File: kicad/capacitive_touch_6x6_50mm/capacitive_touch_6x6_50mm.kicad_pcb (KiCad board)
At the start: 2 copper layers, 50 x 50 mm, 1 part

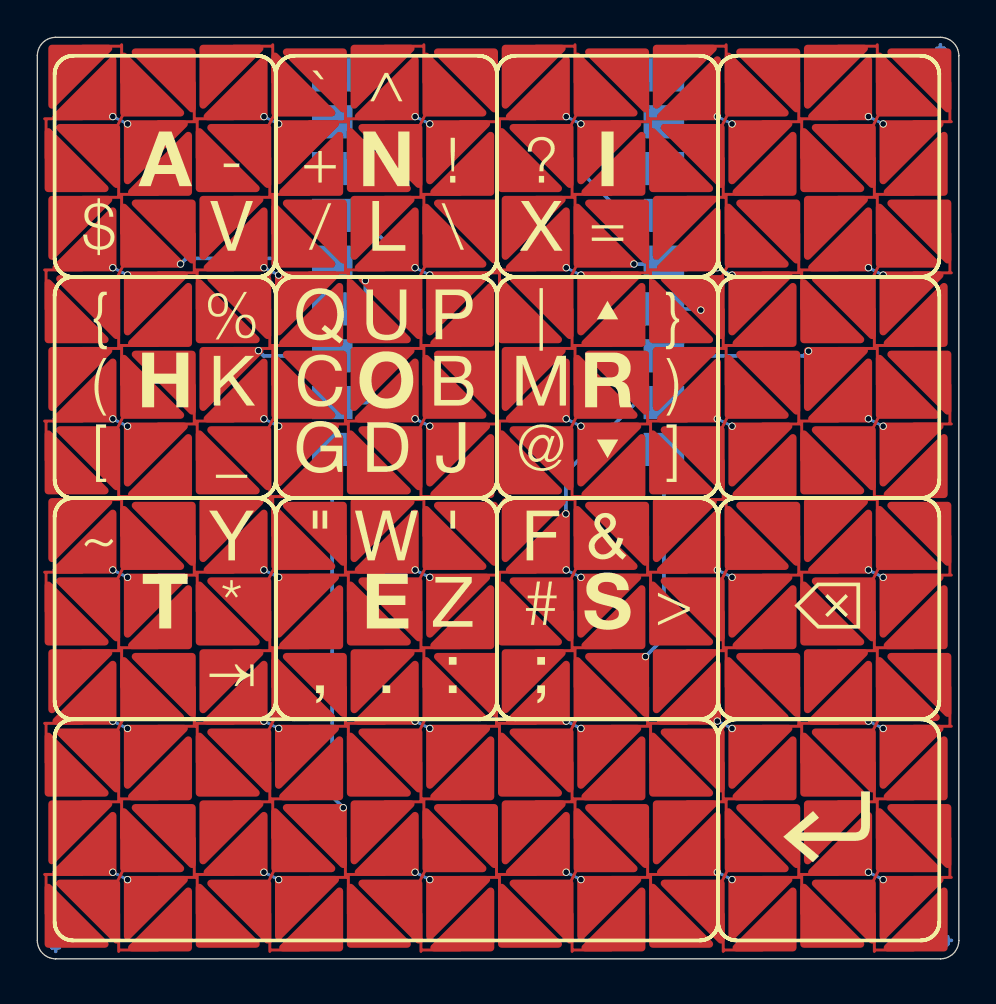
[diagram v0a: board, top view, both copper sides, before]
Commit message: Add QR codes and final graphic changes to pcb
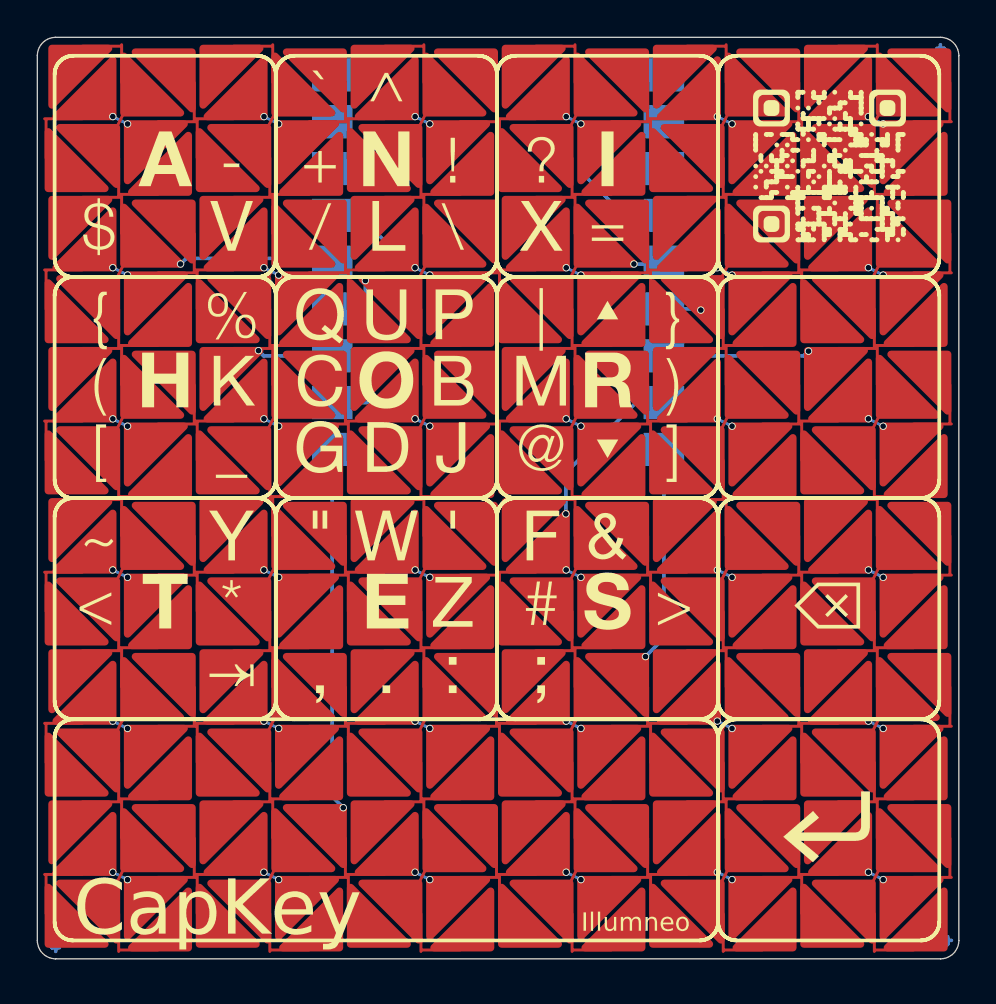
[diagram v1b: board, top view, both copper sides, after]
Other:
- board text added: "2025-10-14"
- board text added: "CapKey"
- board text added: "Designed By: Luke Thompson Illumneo"
- board text added: "Illumneo"
- board text added: "github.com/illumneo/capkey"
- board text added: "tag: supercon2025"
